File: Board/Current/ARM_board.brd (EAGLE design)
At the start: 101.6 x 81.3 mm, 179 parts, among them IC3 STM32F437VI, IC4 LM358DT, J1 USART/I2C, J10 ANALOG, J11 DGND, J12 DPWR, J13 DIGITAL, J14 SGND, J15 SPWR, J16 SERVO, J2 I2C2/USART3, J3 USART2, J5 SPI, J6 Bluesmirf, J7 SWD, J8 AGND, J9 APWR, Q1 STL4P2UH7, Q2 2STR1230, Q3 STL4P2UH7, SW1 SW, U1 LSM330, U10 BAV99, U11 BAV99, U12 USBLC6-2, U13 USBLC6-2, U14 STMPS2171MTR, U15 MC74HC164, U3 NC7SZU04, U4 L6206Q, U5 L6206Q, U6 SI7617, U7 SI7617, U8 SI7617, U9 SI7617, Y2 8MHz

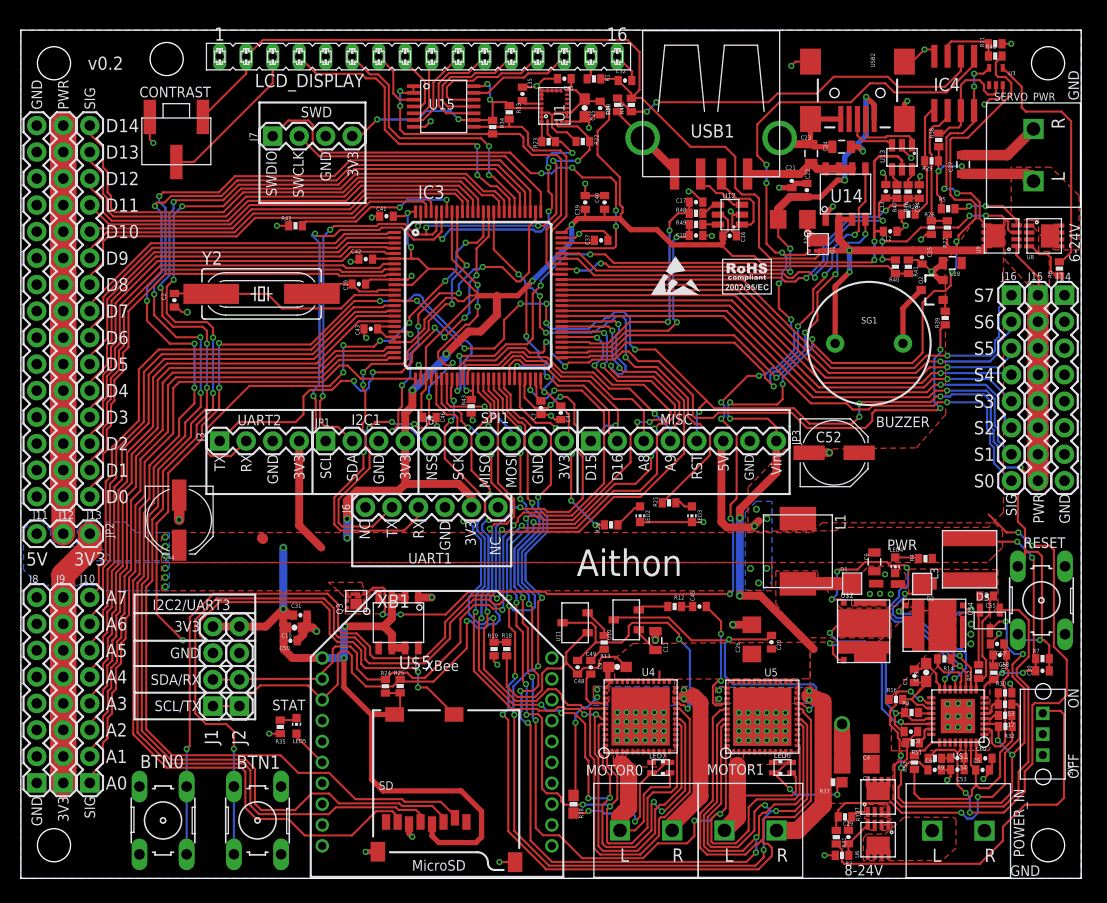
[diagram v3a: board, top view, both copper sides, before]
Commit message: Cleaned up the part numbers of everything but the resistors/caps.
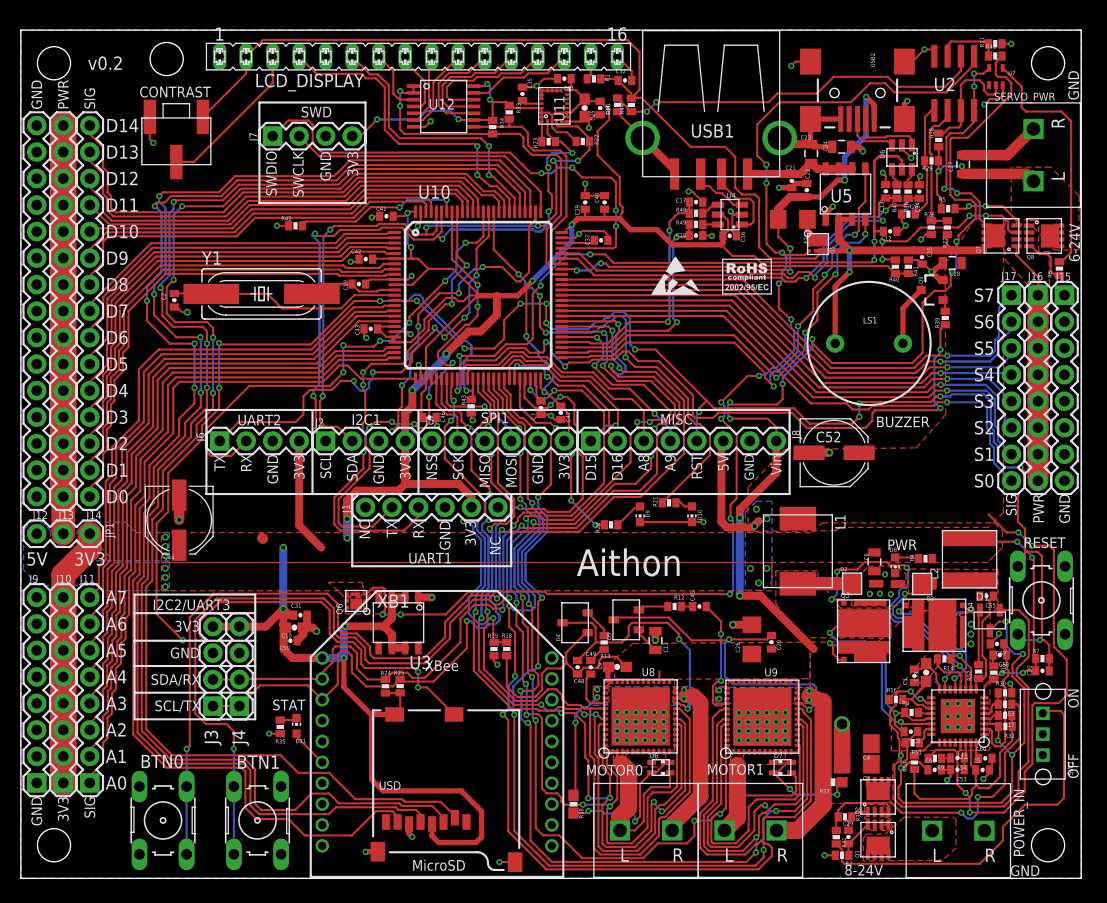
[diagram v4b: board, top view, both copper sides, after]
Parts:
- removed IC3: STM32F437VI, new_parts:TQFP100
- removed JP2: DPWR_SEL, SparkFun:1X03
- removed JP3: MISC, SparkFun:1X08
- removed U$1: PM6685, r_cubed:VFQFPN-32
- removed U$2: DUAL-MOSFET, r_cubed:DUAL-MOSFET-STL60N32N3LL
- removed U$5: LD1117V33, r_cubed:8-SOIC
- removed U13: USBLC6-2, new_parts:SOT23-6L
- removed U14: STMPS2171MTR, r_cubed:8-SOIC
- removed U15: MC74HC164, r_cubed:TSSOP-14
- added D4, D5: BAV99, Parts:SOT-23
- added J17: SERVO, SparkFun:1X08
- added J4: I2C2/USART3, SparkFun:1X04
- added Q5, Q6: STL4P2UH7, r_cubed:POWERFLAT
- added Q7, Q8: SI7617, r_cubed:POWERPAK1212-8
- added Q9: 2STR1230, SparkFun:SOT23-3
- D1: value STPS1L30M -> SOD-23; device SparkFun:STPS1L30M -> r_cubed:SOT-23
- D3: value SOD-23 -> STPS1L30M; device r_cubed:SOT-23 -> SparkFun:STPS1L30M
- J1: value USART/I2C -> Bluesmirf; device SparkFun:1X04 -> SparkFun:1X06
- J10: value ANALOG -> APWR
- J11: value DGND -> ANALOG; device SparkFun:1X15 -> SparkFun:1X08
- J12: value DPWR -> DGND
- J13: value DIGITAL -> DPWR
- J14: value SGND -> DIGITAL; device SparkFun:1X08 -> SparkFun:1X15
- J15: value SPWR -> SGND
- J16: value SERVO -> SPWR
- J2: value I2C2/USART3 -> I2C1
- J3: value USART2 -> USART/I2C
- J6: value Bluesmirf -> USART2; device SparkFun:1X06 -> SparkFun:1X04
- J8: value AGND -> MISC
- J9: value APWR -> AGND
- JP1: value I2C1 -> DPWR_SEL; device SparkFun:1X04 -> SparkFun:1X03
- Q1: value STL4P2UH7 -> SI7617; device r_cubed:POWERFLAT -> r_cubed:POWERPAK1212-8
- Q2: value 2STR1230 -> SI7617; device SparkFun:SOT23-3 -> r_cubed:POWERPAK1212-8
- Q3: value STL4P2UH7 -> DUAL-MOSFET; device r_cubed:POWERFLAT -> r_cubed:DUAL-MOSFET-STL60N32N3LL
- U1: value LSM330 -> PM6685; device r_cubed:LSM330 -> r_cubed:VFQFPN-32
- U10: value BAV99 -> STM32F437VI; device Parts:SOT-23 -> new_parts:TQFP100
- U11: value BAV99 -> LSM330; device Parts:SOT-23 -> r_cubed:LSM330
- U12: value USBLC6-2 -> MC74HC164; device new_parts:SOT23-6L -> r_cubed:TSSOP-14
- U3: value NC7SZU04 -> LD1117V33; device SparkFun:SC70 -> r_cubed:8-SOIC
- U4: value L6206Q -> USBLC6-2; device r_cubed:VFQFPN48 -> new_parts:SOT23-6L
- U5: value L6206Q -> STMPS2171MTR; device r_cubed:VFQFPN48 -> r_cubed:8-SOIC
- U6: value SI7617 -> USBLC6-2; device r_cubed:POWERPAK1212-8 -> new_parts:SOT23-6L
- U7: value SI7617 -> NC7SZU04; device r_cubed:POWERPAK1212-8 -> SparkFun:SC70
- U8, U9: value SI7617 -> L6206Q; device r_cubed:POWERPAK1212-8 -> r_cubed:VFQFPN48
- moved J14 95.4 mm to (6.60, 36.6), turned to 90 degrees
- moved U3 76.7 mm to (36.8, 25.1), turned to 180 degrees
- moved U1 70.1 mm to (89.8, 15.6), turned to 180 degrees
- moved U7 70.0 mm to (93.4, 76.8), turned to 0 degrees
- moved U6 65.5 mm to (84.5, 69.1)
- moved J8 62.4 mm to (54.6, 41.9), turned to 0 degrees
- moved U8 60.1 mm to (59.4, 15.5), turned to 90 degrees
- moved Q1 57.4 mm to (82.1, 3.71)
- moved U9 51.5 mm to (71.0, 15.5), turned to 90 degrees
- moved U5 50.0 mm to (78.4, 64.9), turned to 0 degrees
- moved U11 49.6 mm to (51.1, 74.0)
- moved Q2 48.9 mm to (82.1, 7.80)
- moved U4 48.8 mm to (68.0, 63.6), turned to 180 degrees
- moved Q3 48.7 mm to (80.8, 23.1), turned to 0 degrees
- moved U10 34.2 mm to (43.8, 55.9), turned to 0 degrees
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- renumbered IC4 to U2, L3 to L2, LED2 to D9, LED3 to D10, LED4 to D8, LED5 to D11, LED6 to D7, LED7 to D6, SD to USD, SG1 to LS1, U$4 to Q4, Y2 to Y1
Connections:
- net +3V3: now also J1.5, J10.1, J10.2, J10.3, J10.4, J10.5, J10.6, J10.7, J10.8, J4.4, J6.4, JP1.1, U10.100, U10.11, U10.19, U10.21, U10.22, U10.28, U10.50, U10.6, U10.75, U11.1, U11.13, U11.22, U11.23, U11.24, U11.3, U11.7, U11.8, U12.14, U12.9, U3.2, U3.3, U3.6, U3.7, U4.P$5, U6.P$5; no longer IC3.100, IC3.11, IC3.19, IC3.21, IC3.22, IC3.28, IC3.50, IC3.6, IC3.75, J1.4, J6.5, J9.1, J9.2, J9.3, J9.4, J9.5, J9.6, J9.7, J9.8, JP1.4, JP2.1, U$1.8, U$5.2, U$5.3, U$5.6, U$5.7, U1.1, U1.13, U1.22, U1.23, U1.24, U1.3, U1.7, U12.P$5, U13.P$5, U15.14, U15.9
- net 5V: now also J8.6, JP1.3, Q5.4, Q5.7, Q6.4, Q6.7, Q7.5, Q7.6, Q7.7, Q7.8, Q7.PAD, U1.29, U5.2, U5.3, U7.5; no longer JP2.3, JP3.6, Q1.4, Q1.7, Q3.4, Q3.7, U$1.29, U14.2, U14.3, U3.5, U9.5, U9.6, U9.7, U9.8, U9.PAD
- net ANALOG0: now also J11.1, U10.26; no longer IC3.26, J10.1
- net ANALOG1: now also J11.2, U10.25; no longer IC3.25, J10.2
- net ANALOG2: now also J11.3, U10.24; no longer IC3.24, J10.3
- net ANALOG3: now also J11.4, U10.23; no longer IC3.23, J10.4
- net ANALOG4: now also J11.5, U10.18; no longer IC3.18, J10.5
- net ANALOG5: now also J11.6, U10.17; no longer IC3.17, J10.6
- net ANALOG6: now also J11.7, U10.16; no longer IC3.16, J10.7
- net ANALOG7: now also J11.8, U10.15; no longer IC3.15, J10.8
- net ANALOG8: now also J8.3, U10.36; no longer IC3.36, JP3.3
- net ANALOG9: now also J8.4, U10.35; no longer IC3.35, JP3.4
- net BAT_SENSE: now also U10.33; no longer IC3.33
- net BOOT1: now also U10.37; no longer IC3.37
- net BOOT3: now also D1.P$2; no longer D3.P$2
- net BTN0: now also U10.57; no longer IC3.57
- net BTN1: now also U10.58; no longer IC3.58
- net BUZZER: now also U10.29; no longer IC3.29
- net DIGITAL0: now also J14.1, U10.9; no longer IC3.9, J13.1
- net DIGITAL1: now also J14.2, U10.8; no longer IC3.8, J13.2
- net DIGITAL10: now also J14.11, U10.91; no longer IC3.91, J13.11
- net DIGITAL11: now also J14.12, U10.90; no longer IC3.90, J13.12
- net DIGITAL12: now also J14.13, U10.89; no longer IC3.89, J13.13
- net DIGITAL13: now also J14.14, U10.88; no longer IC3.88, J13.14
- net DIGITAL14: now also J14.15, U10.84; no longer IC3.84, J13.15
- net DIGITAL15: now also J8.1, U10.44; no longer IC3.44, JP3.1
- net DIGITAL16: now also J8.2, U10.45; no longer IC3.45, JP3.2
- net DIGITAL2: now also J14.3, U10.7; no longer IC3.7, J13.3
- net DIGITAL3: now also J14.4, U10.5; no longer IC3.5, J13.4
- net DIGITAL4: now also J14.5, U10.4; no longer IC3.4, J13.5
- net DIGITAL5: now also J14.6, U10.3; no longer IC3.3, J13.6
- net DIGITAL6: now also J14.7, U10.2; no longer IC3.2, J13.7
- net DIGITAL7: now also J14.8, U10.1; no longer IC3.1, J13.8
- net DIGITAL8: now also J14.9, U10.98; no longer IC3.98, J13.9
- net DIGITAL9: now also J14.10, U10.97; no longer IC3.97, J13.10
- net GND: now also D3.P$1, J1.4, J12.1, J12.10, J12.11, J12.12, J12.13, J12.14, J12.15, J12.2, J12.3, J12.4, J12.5, J12.6, J12.7, J12.8, J12.9, J15.1, J15.2, J15.3, J15.4, J15.5, J15.6, J15.7, J15.8, J4.3, J6.3, J9.1, J9.2, J9.3, J9.4, J9.5, J9.6, J9.7, J9.8, Q3.5/6/7, Q9.2, U1.1, U1.24, U1.28, U1.PAD, U10.10, U10.20, U10.27, U10.74, U10.99, U11.14, U11.15, U11.16, U11.17, U11.18, U11.19, U11.20, U11.5, U11.6, U12.7, U3.1, U4.P$2, U6.P$2, U7.3, U8.1, U8.12, U8.14, U8.15, U8.16, U8.19, U8.24, U8.25, U8.28, U8.29, U8.30, U8.31, U8.32, U8.33, U8.36, U8.37, U8.4, U8.42, U8.45, U8.46, U8.47, U8.5, U8.6, U8.7, U8.8, U8.9, U8.PAD, U9.1, U9.12, U9.14, U9.15, U9.16, U9.19, U9.24, U9.25, U9.28, U9.29, U9.30, U9.31, U9.32, U9.33, U9.36, U9.37, U9.4, U9.42, U9.45, U9.46, U9.47, U9.5, U9.6, U9.7, U9.8, U9.9, U9.PAD; no longer D1.P$1, IC3.10, IC3.20, IC3.27, IC3.74, IC3.99, J1.3, J11.1, J11.10, J11.11, J11.12, J11.13, J11.14, J11.15, J11.2, J11.3, J11.4, J11.5, J11.6, J11.7, J11.8, J11.9, J14.1, J14.2, J14.3, J14.4, J14.5, J14.6, J14.7, J14.8, J6.4, J8.1, J8.2, J8.3, J8.4, J8.5, J8.6, J8.8, JP1.3, JP3.7, Q2.2, U$1.1, U$1.14, U$1.16, U$1.17, U$1.24, U$1.28, U$1.PAD, U$2.5/6/7, U$5.1, U1.15, U1.18, U1.19, U1.20, U1.5, U1.6, U12.P$2, U13.P$2, U14.1, U15.7, U3.3, U4.1, U4.12, U4.14, U4.15, U4.16, U4.19, U4.24, U4.25, U4.28, U4.29, U4.30, U4.31, U4.32, U4.33, U4.36, U4.37, U4.4, U4.42, U4.45, U4.46, U4.47, U4.5, U4.6, U4.7, U4.8, U4.9, U4.PAD, U5.12, U5.14, U5.15, U5.16, U5.19, U5.24, U5.25, U5.28, U5.29, U5.30, U5.31, U5.32, U5.33, U5.36, U5.37, U5.4, U5.42, U5.45, U5.46, U5.47, U5.5, U5.6, U5.7, U5.8, U5.9, U5.PAD
- net I2C1_SCL: now also J2.1, U10.95, U11.2; no longer IC3.95, JP1.1, U1.2
- net I2C1_SDA: now also J2.2, U10.96, U11.4; no longer IC3.96, JP1.2, U1.4
- net I2C2_SCL/USART3_TX: now also J3.1, J4.1, U10.47; no longer IC3.47, J1.1, J2.1
- net I2C2_SDA/USART3_RX: now also J3.2, J4.2, U10.48; no longer IC3.48, J1.2, J2.2
- net LCD_CLK: now also U10.69, U12.8; no longer IC3.69, U15.8
- net LCD_DATA: now also U10.67, U12.1, U12.2; no longer IC3.67, U15.1, U15.2
- net LCD_E: now also U10.81; no longer IC3.81
- net LCD_RS: now also U10.82; no longer IC3.82
- net LDO5: now also D1.P$0, U1.18, U1.3; no longer D3.P$0, U$1.18, U$1.3
- net LED0: now also U10.46; no longer IC3.46
- net LED1: now also U10.85; no longer IC3.85
- net M0_A: now also U10.38, U8.17, U8.43; no longer IC3.38, U4.17, U4.43
- net M0_B: now also U10.39, U8.18, U8.44; no longer IC3.39, U4.18, U4.44
- net M0_EN: now also U10.40, U8.20, U8.41; no longer IC3.40, U4.20, U4.41
- net M0_FAULT: now also U10.55, U8.13, U8.48; no longer IC3.55, U4.13, U4.48
- net M1_A: now also U10.41, U9.17, U9.43; no longer IC3.41, U5.17, U5.43
- net M1_B: now also U10.43, U9.18, U9.44; no longer IC3.43, U5.18, U5.44
- net M1_EN: now also U10.42, U9.20, U9.41; no longer IC3.42, U5.20, U5.41
- net M1_FAULT: now also U10.56, U9.13, U9.48; no longer IC3.56, U5.13, U5.48
- net N$1: now also Q1.5, Q1.6, Q1.7, Q1.8, Q1.PAD; no longer U6.5, U6.6, U6.7, U6.8, U6.PAD
- net N$11: now also U11.21; no longer U1.21
- net N$13: now also U4.P$3; no longer U12.P$3
- net N$14: now also Q5.3, Q6.3; no longer Q1.3, Q3.3
- net N$15: now also U1.31; no longer U$1.31
- net N$16: now also U4.P$1; no longer U12.P$1
- net N$17: now also U6.P$1; no longer U13.P$1
- net N$19: now also J13.1, J13.10, J13.11, J13.12, J13.13, J13.14, J13.15, J13.2, J13.3, J13.4, J13.5, J13.6, J13.7, J13.8, J13.9, JP1.2; no longer J12.1, J12.10, J12.11, J12.12, J12.13, J12.14, J12.15, J12.2, J12.3, J12.4, J12.5, J12.6, J12.7, J12.8, J12.9, JP2.2
- net N$2: now also Q1.4; no longer U6.4
- net N$20: now also U1.23; no longer U$1.23
- net N$21: now also U5.6, U5.7, U5.8; no longer U14.6, U14.7, U14.8
- net N$22: now also Q6.1, Q6.2, Q6.5, Q6.6, Q6.8, U3.4; no longer Q3.1, Q3.2, Q3.5, Q3.6, Q3.8, U$5.4
- net N$23: now also Q1.1, Q1.2, Q1.3, Q2.1, Q2.2, Q2.3; no longer U6.1, U6.2, U6.3, U7.1, U7.2, U7.3
- net N$24: now also U10.49; no longer IC3.49
- net N$25: now also D1.P$1; no longer D3.P$1
- net N$27: now also U7.2; no longer U3.2
- net N$28: now also Q9.3; no longer Q2.3
- net N$3: now also U10.94; no longer IC3.94
- net N$30: now also U7.4; no longer U3.4
- net N$32: now also Q5.1, Q5.2, Q5.5, Q5.6, Q5.8; no longer Q1.1, Q1.2, Q1.5, Q1.6, Q1.8
- net N$33: now also U6.P$4; no longer U13.P$4
- net N$34: now also U4.P$4; no longer U12.P$4
- net N$36: now also U4.P$6; no longer U12.P$6
- net N$38: now also U9.40; no longer U5.40
- net N$39: now also D5.3, U9.21; no longer U10.3, U5.21
- net N$4: now also U10.73; no longer IC3.73
- net N$40: now also D5.2; no longer U10.2
- net N$44: now also U1.13; no longer U$1.13
- net N$45: now also U8.40; no longer U4.40
- net N$46: now also U10.12; no longer IC3.12
- net N$47: now also U10.13; no longer IC3.13
- net N$48: now also D4.3, U8.21; no longer U11.3, U4.21
- net N$49: now also D4.2; no longer U11.2
- net N$50: now also Q7.4; no longer U9.4
- net N$53: now also Q8.4; no longer U8.4
- net N$55: now also U1.20; no longer U$1.20
- net N$56: now also Q3.1, U1.22; no longer U$1.22, U$2.1
- net N$57: now also Q3.8, U1.15; no longer U$1.15, U$2.8
- net N$58: now also U12.3; no longer U15.3
- net N$59: now also U1.9; no longer U$1.9
- net N$6: now also U6.P$6; no longer U13.P$6
- net N$60: now also U12.4; no longer U15.4
- net N$61: now also U12.5; no longer U15.5
- net N$62: now also U12.6; no longer U15.6
- net N$63: now also U12.10; no longer U15.10
- net N$64: now also U12.11; no longer U15.11
- net N$65: now also Q9.1; no longer Q2.1
- net N$66: now also D2.C2, D2.P$2, Q3.S1D2, U1.21; no longer D1.C2, D1.P$2, U$1.21, U$2.S1D2
- net N$68: now also Q2.4; no longer U7.4
- net N$69: now also U1.30; no longer U$1.30
- net N$7: now also U1.32; no longer U$1.32
- net N$70: now also U12.12; no longer U15.12
- net N$71: now also U12.13; no longer U15.13
- net N$73: now also U1.10; no longer U$1.10
- net N$75: now also D3.C2, D3.P$2, U1.11; no longer D2.C2, D2.P$2, U$1.11
- net N$76: now also U1.12; no longer U$1.12
- net N$77: now also U1.2; no longer U$1.2
- net N$79: now also U1.19; no longer U$1.19
- net N$8: now also U6.P$3; no longer U13.P$3
- net N$82: now also U1.5; no longer U$1.5
- net N$83: now also U1.4; no longer U$1.4
- net N$84: now also U1.25; no longer U$1.25
- net OUT1: now also U8.10, U8.11, U8.2, U8.3; no longer U4.10, U4.11, U4.2, U4.3
- net OUT2: now also U8.22, U8.23, U8.38, U8.39; no longer U4.22, U4.23, U4.38, U4.39
- net OUT3: now also U9.10, U9.11, U9.2, U9.3; no longer U5.10, U5.11, U5.2, U5.3
- net OUT4: now also U9.22, U9.23, U9.38, U9.39; no longer U5.22, U5.23, U5.38, U5.39
- net RAW_SPWR: now also Q8.5, Q8.6, Q8.7, Q8.8, Q8.PAD; no longer U8.5, U8.6, U8.7, U8.8, U8.PAD
- net RESET: now also J8.5, U10.14; no longer IC3.14, JP3.5
- net SERVO0: now also J17.8, U10.59; no longer IC3.59, J16.8
- net SERVO1: now also J17.7, U10.60; no longer IC3.60, J16.7
- net SERVO2: now also J17.6, U10.61; no longer IC3.61, J16.6
- net SERVO3: now also J17.5, U10.62; no longer IC3.62, J16.5
- net SERVO4: now also J17.4, U10.63; no longer IC3.63, J16.4
- net SERVO5: now also J17.3, U10.64; no longer IC3.64, J16.3
- net SERVO6: now also J17.2, U10.65; no longer IC3.65, J16.2
- net SERVO7: now also J17.1, U10.66; no longer IC3.66, J16.1
- net SERVO_SENSE: now also U10.34; no longer IC3.34
- net SPI1_MISO: now also U10.31; no longer IC3.31
- net SPI1_MOSI: now also U10.32; no longer IC3.32
- net SPI1_NSS: now also U10.77; no longer IC3.77
- net SPI1_SCK: now also U10.30; no longer IC3.30
- net SPI3_MISO: now also U10.79; no longer IC3.79
- net SPI3_MOSI: now also U10.80; no longer IC3.80
- net SPI3_NSS: now also U10.83; no longer IC3.83
- net SPI3_SCK: now also U10.78; no longer IC3.78
- net SPWR: now also J16.1, J16.2, J16.3, J16.4, J16.5, J16.6, J16.7, J16.8, Q7.1, Q7.2, Q7.3, Q8.1, Q8.2, Q8.3; no longer J15.1, J15.2, J15.3, J15.4, J15.5, J15.6, J15.7, J15.8, U8.1, U8.2, U8.3, U9.1, U9.2, U9.3
- net SWDCLK: now also U10.76; no longer IC3.76
- net SWDIO: now also U10.72; no longer IC3.72
- net USART1_RX: now also J1.3, U10.93; no longer IC3.93, J6.3
- net USART1_TX: now also J1.2, U10.92; no longer IC3.92, J6.2
- net USART2_RX: now also J6.2, U10.87; no longer IC3.87, J3.2
- net USART2_TX: now also J6.1, U10.86; no longer IC3.86, J3.1
- net USB_5V: now also U10.68; no longer IC3.68
- net USB_DEV_DM: now also U10.70; no longer IC3.70
- net USB_DEV_DP: now also U10.71; no longer IC3.71
- net USB_HOST_DM: now also U10.53; no longer IC3.53
- net USB_HOST_DP: now also U10.54; no longer IC3.54
- net USB_HOST_EN: now also U10.52, U5.4; no longer IC3.52, U14.4
- net USB_HOST_FAULT: now also U10.51, U5.5; no longer IC3.51, U14.5
- net VIN: now also D4.1, D5.1, J8.8, Q2.5, Q2.6, Q2.7, Q2.8, Q2.PAD, Q3.2/3/4, Q3.D1, U8.26, U8.27, U8.34, U8.35, U9.26, U9.27, U9.34, U9.35; no longer JP3.8, U$2.2/3/4, U$2.D1, U10.1, U11.1, U4.26, U4.27, U4.34, U4.35, U5.26, U5.27, U5.34, U5.35, U7.5, U7.6, U7.7, U7.8, U7.PAD

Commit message: Made some minor tweaks to the schematic and layout while creating the BOM.
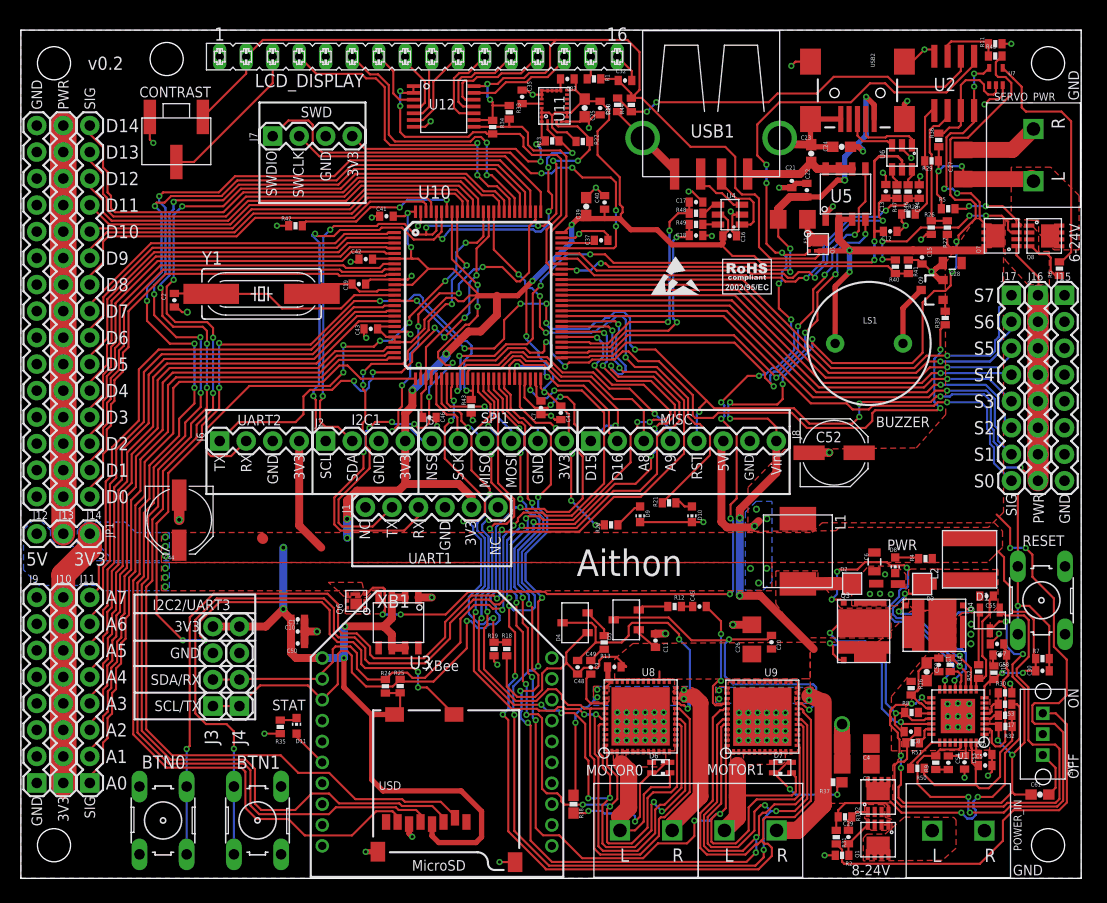
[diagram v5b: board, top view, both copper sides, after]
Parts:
- C10, C9: device SparkFun:0603-CAP -> SparkFun:0402-CAP
- C11: device SparkFun:0805 -> SparkFun:0402-CAP
- C23, C24: device SparkFun:0805 -> SparkFun:0603-CAP
- C27: device SparkFun:0805 -> SparkFun:1206
- C39, C61: device SparkFun:0402-CAP -> SparkFun:0603-CAP
- C44, C52: value 680uF -> 470u
- C50: value 8.2p -> 20p
- D1: value SOD-23 -> BAS70-06FILM
- D4: value BAV99 -> BAS70-05FILM
- D6, D7: value LED_R/G -> RED/GRN
- J3: value USART/I2C -> I2C2/USART3
- U3: value LD1117V33 -> LD1117D33TR
- moved C61 10.4 mm to (97.7, 8.03)
- moved C1 2.56 mm to (88.0, 20.5), turned to 270 degrees
- moved R16 1.82 mm to (85.3, 18.2), turned to 270 degrees
- moved C31 1.59 mm to (26.5, 23.7)
- moved C53 0.98 mm to (90.4, 11.1), turned to 270 degrees
- moved C54 0.98 mm to (88.9, 11.1), turned to 270 degrees
- moved C10 0.85 mm to (26.5, 24.8)
- moved R14 0.79 mm to (89.1, 20.5), turned to 270 degrees
- moved C50 0.75 mm to (26.5, 22.5)
- moved R50 0.63 mm to (85.9, 10.5), turned to 180 degrees
- moved C5 0.49 mm to (92.4, 10.8)
- moved R9 0.43 mm to (87.7, 11.1), turned to 90 degrees
- moved C39 0.41 mm to (54.2, 64.4)
- moved C60 0.36 mm to (92.4, 11.9)
- moved R23 0.35 mm to (50.9, 70.7)
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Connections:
- net +3V3: no longer R33.1, R34.1, U12.14, U12.9
- net 5V: now also R33.1, R34.1, U12.14, U12.9
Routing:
- net 5V: track 204.8 -> 231.7 mm, vias 19 -> 21
- net +3V3: track 372.1 -> 363.2 mm, vias 27 -> 23
- net N$25: track 41.6 -> 48.0 mm
- net GND: track 155.4 -> 150.7 mm
- net N$15: track 22.8 -> 19.9 mm
- net N$70: track 13.6 -> 10.8 mm
- net N$64: track 12.5 -> 9.74 mm
- net N$63: track 11.3 -> 8.77 mm
- net LDO5: track 54.8 -> 52.6 mm
- net N$76: track 4.71 -> 2.61 mm
- net RESET: track 111.8 -> 110.0 mm
- net N$79: track 6.58 -> 7.92 mm
- net N$84: track 2.94 -> 4.07 mm
- net LCD_E: track 26.4 -> 27.5 mm
- net LCD_RS: track 31.0 -> 31.9 mm
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
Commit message: Made tweaks to schematic / layout.
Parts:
- moved U3 0.70 mm to (36.8, 24.4)
- moved R24 0.41 mm to (35.0, 18.0)
- moved R25 0.41 mm to (36.3, 18.0)
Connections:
- net +3V3: now also USD.CD2
- net BOOT1: now also USD.GND1; no longer USD.CD2
- net GND: no longer USD.GND1
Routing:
- net BOOT1: track 104.5 -> 117.5 mm, vias 8 -> 6
- net USART1_RX: track 52.1 -> 39.1 mm, vias 8 -> 6
- net USART1_TX: track 44.6 -> 37.1 mm
- net N$14: track 119.4 -> 115.6 mm, vias 12 -> 10
- net +3V3: track 363.2 -> 359.8 mm, vias 23 -> 21
- net SPI3_MISO: track 130.4 -> 132.6 mm
- net BAT_SENSE: track 34.3 -> 32.3 mm
- net GND: track 150.7 -> 152.6 mm, vias 116 -> 114
- net BTN1: track 116.1 -> 117.6 mm
- net SPI3_SCK: track 131.7 -> 133.2 mm
- net BTN0: track 110.0 -> 111.2 mm
- net SPI1_NSS: track 36.7 -> 35.7 mm
- net I2C2_SCL/USART3_TX: track 76.2 -> 75.2 mm
- net M1_B: track 113.8 -> 114.6 mm
- net M1_EN: track 118.3 -> 119.0 mm
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
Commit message: Final layout tweaks.
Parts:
- moved R20 1.60 mm to (57.4, 35.2)
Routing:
- net +3V3: track 359.8 -> 361.3 mm
- net LED0: track 20.1 -> 21.5 mm
- net N$42: track 2.86 -> 1.44 mm
- net 5V: track 231.7 -> 230.5 mm
- net SPI1_NSS: track 35.7 -> 36.5 mm
- net LED1: track 46.5 -> 47.2 mm
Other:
- board text added: "LED0"
- board text added: "LED1"
